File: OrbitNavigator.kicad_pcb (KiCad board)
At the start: 2 copper layers, 1 part, among them U1 STM32G474RET6

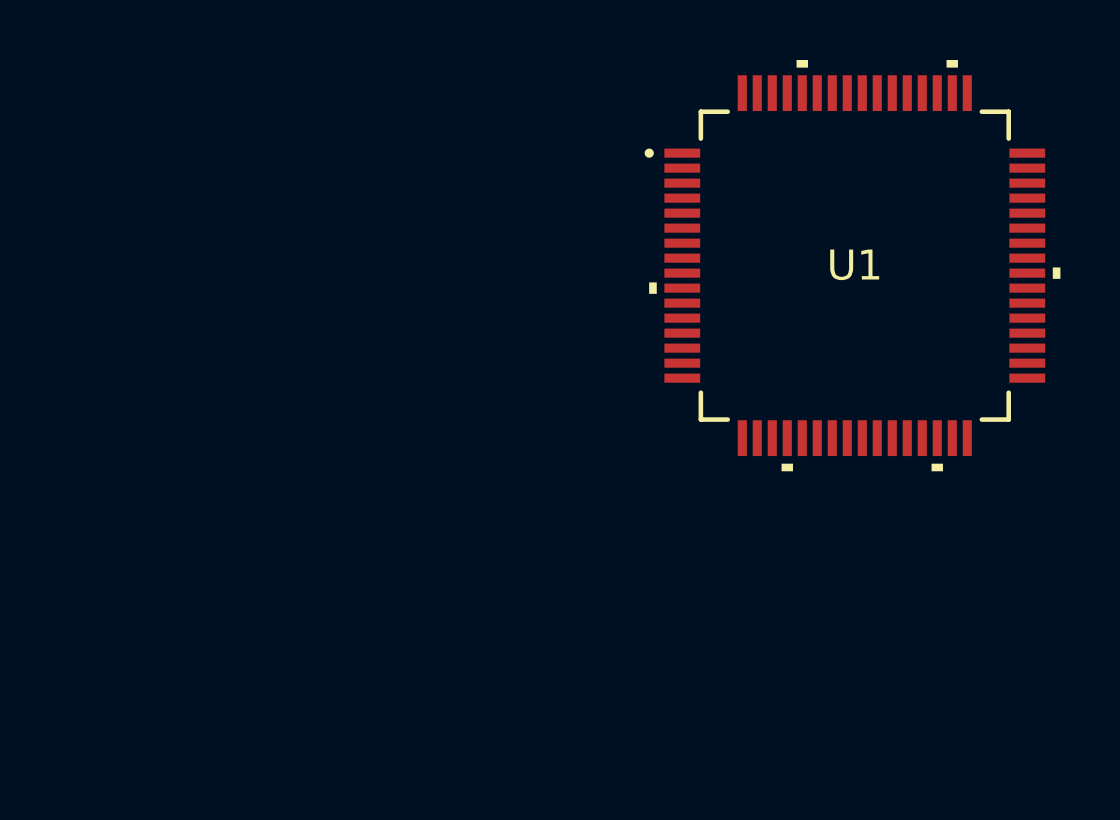
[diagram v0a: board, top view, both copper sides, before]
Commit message: Sensor and MCU Schematic Done
Added
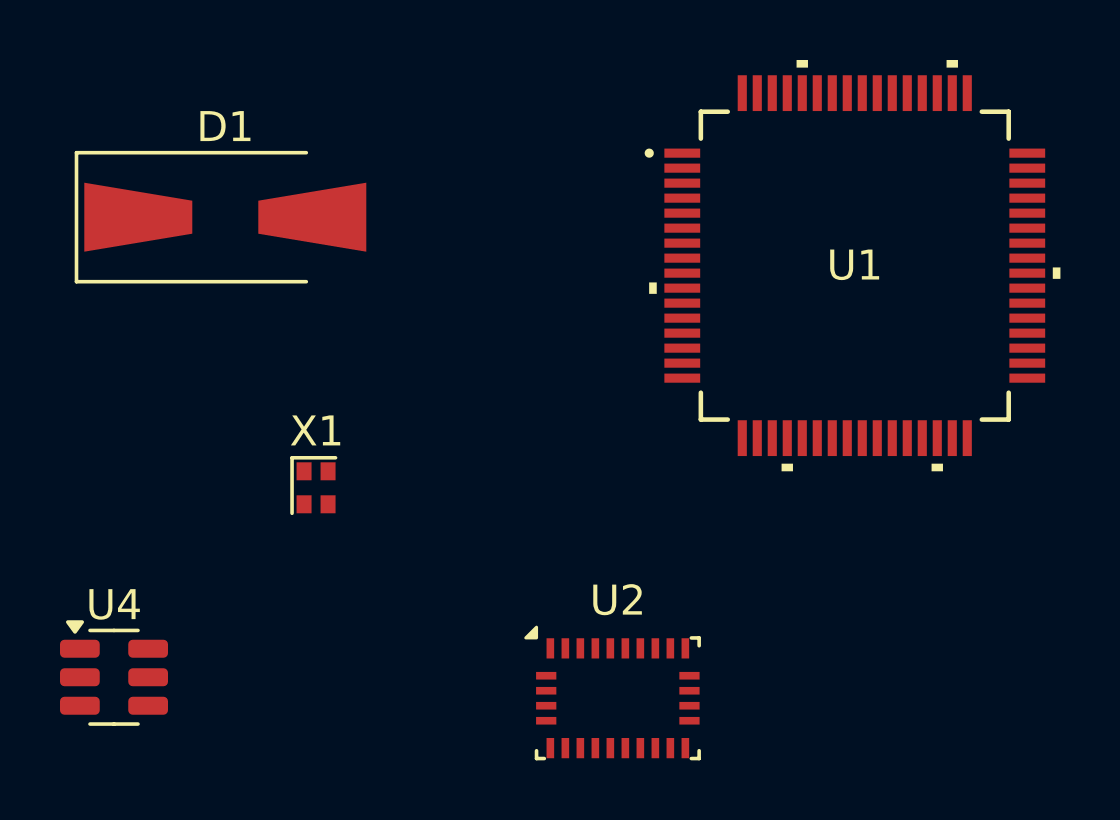
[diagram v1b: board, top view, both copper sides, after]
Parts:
- added D1: SM6T6V8A, Diode_SMD:D_SMA-SMB_Universal_Handsoldering, F.Cu at (63.3, 42.1)
- added U2: BNO055, Package_LGA:LGA-28_5.2x3.8mm_P0.5mm, F.Cu at (76.4, 58.2)
- added U4: USBLC6-2SC6, Package_TO_SOT_SMD:SOT-23-6, F.Cu at (59.6, 57.5)
- added X1: ASCO, Oscillator:Oscillator_SMD_Abracon_ASCO-4Pin_1.6x1.2mm, F.Cu at (66.3, 51.2)
